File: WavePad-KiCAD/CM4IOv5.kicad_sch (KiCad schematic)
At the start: 8 parts

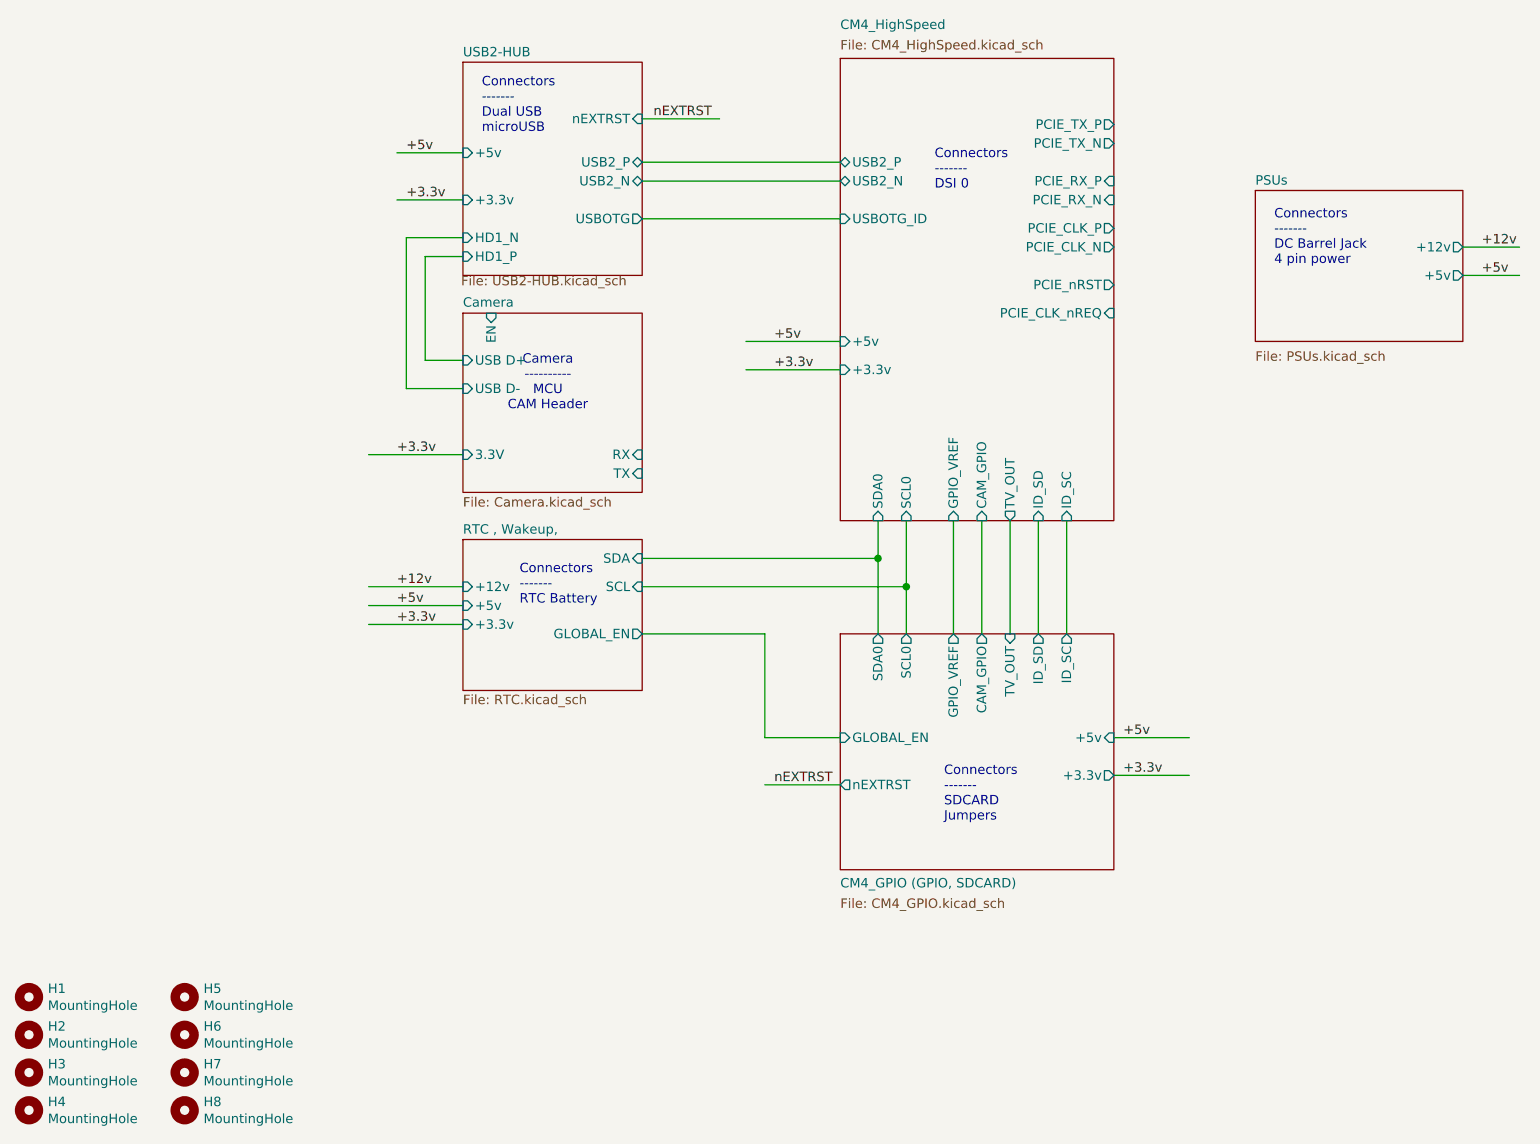
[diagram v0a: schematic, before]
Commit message: Started PCB
Added CSI and DSI connector as well as a USB C with protected  data and Power
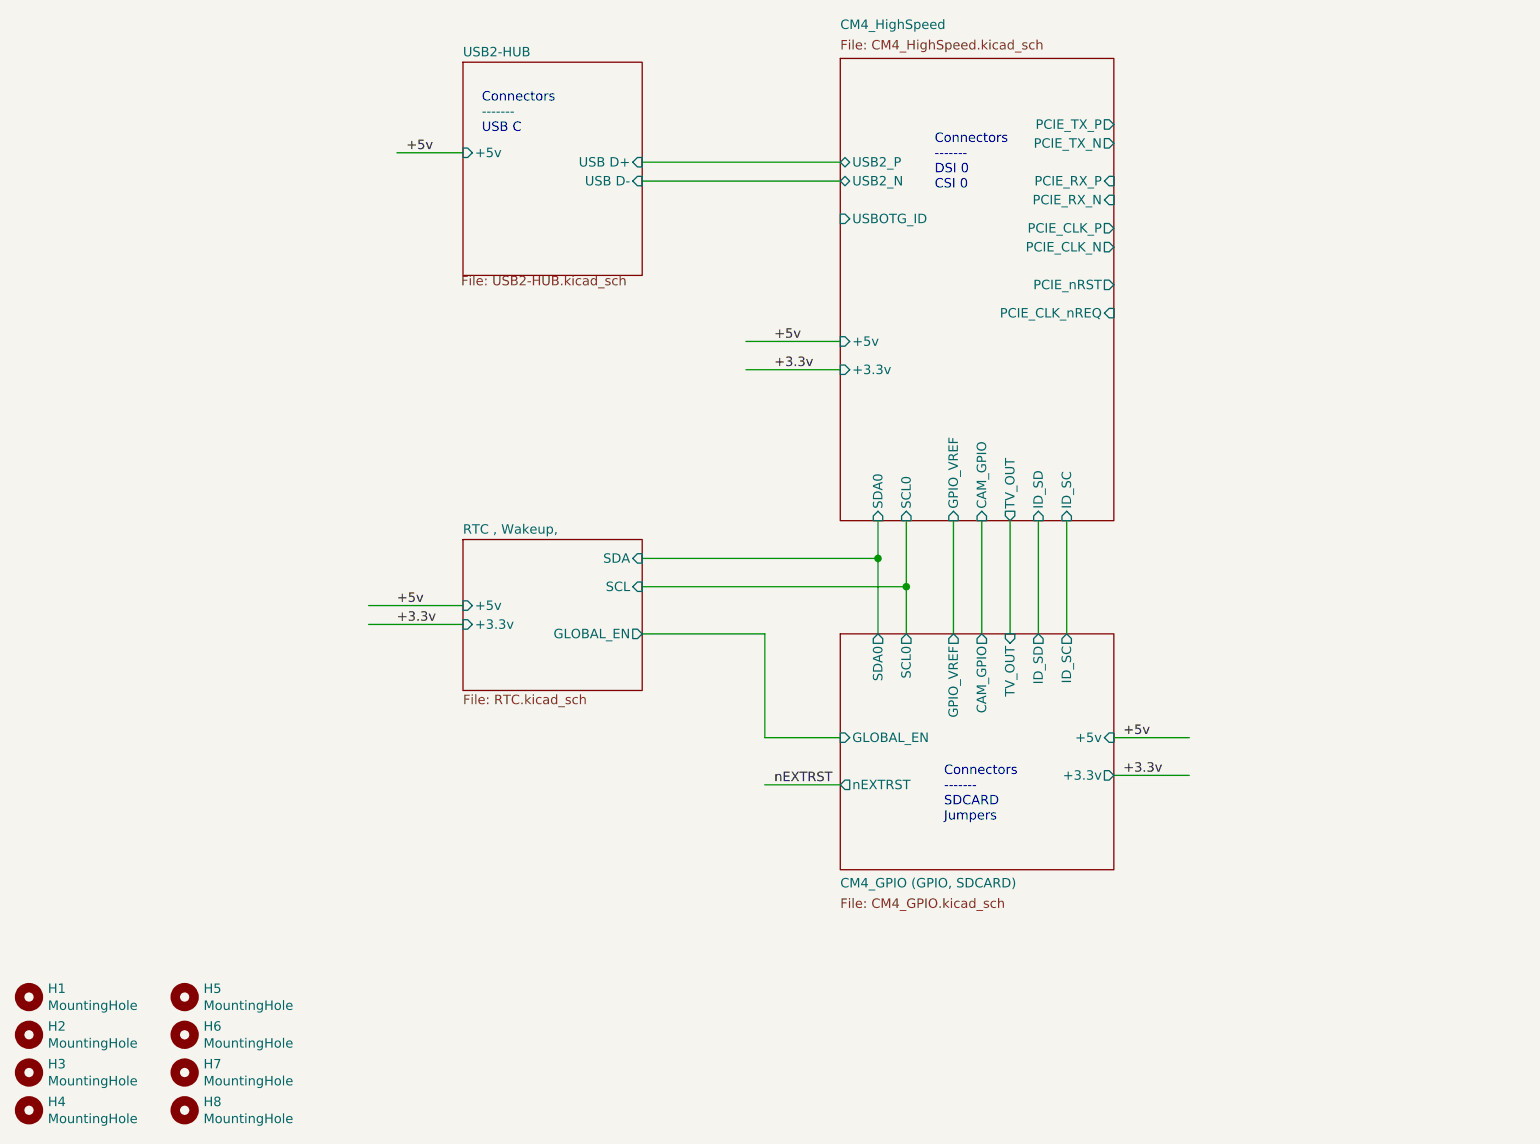
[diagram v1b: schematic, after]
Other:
- removed sheet Camera
- removed sheet PSUs
- sheet RTC , Wakeup, ports: added none; removed +12v
- sheet USB2-HUB ports: added USB D+, USB D-; removed +3.3v, HD1_N, HD1_P, USB2_N, USB2_P, USBOTG, nEXTRST
- note added: "Connectors ------- DSI 0 CSI 0"
- note added: "Connectors ------- USB C"
- note removed: "Camera ---------- MCU CAM Header"
- note removed: "Connectors ------- DC Barrel Jack 4 pin power"
- note removed: "Connectors ------- DSI 0"
- note removed: "Connectors ------- Dual USB microUSB"
- note removed: "Connectors ------- RTC Battery"

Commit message: Worked on PCB
Almost finished the PCB
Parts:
- removed H5, H6, H7, H8: MountingHole, MountingHole:MountingHole_2.7mm_M2.5, symbol Mechanical:MountingHole
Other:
- sheet USB2-HUB renamed USB
- removed sheet RTC , Wakeup,
- sheet USB: file USB2-HUB.kicad_sch -> USB.kicad_sch
